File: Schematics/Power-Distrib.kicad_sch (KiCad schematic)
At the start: 43 parts, among them J10 Screw_Terminal_01x02, J11 Screw_Terminal_01x02, J12 Screw_Terminal_01x02, J13 Conn_01x03, J14 Conn_01x03, J15 Conn_01x03, J16 Conn_01x03, J17 Conn_01x02, J18 Conn_01x02, J19 Conn_01x02, J20 Conn_01x02, J21 Conn_01x02, J22 Conn_01x02, J23 Conn_01x02, J24 Conn_01x02, J25 Conn_01x03, J26 Conn_01x03, J27 Conn_01x03, J28 Conn_01x03, J29 Conn_01x03, U15 LM7805, U16 LM7812, U17 LM7912, U18 LM7805

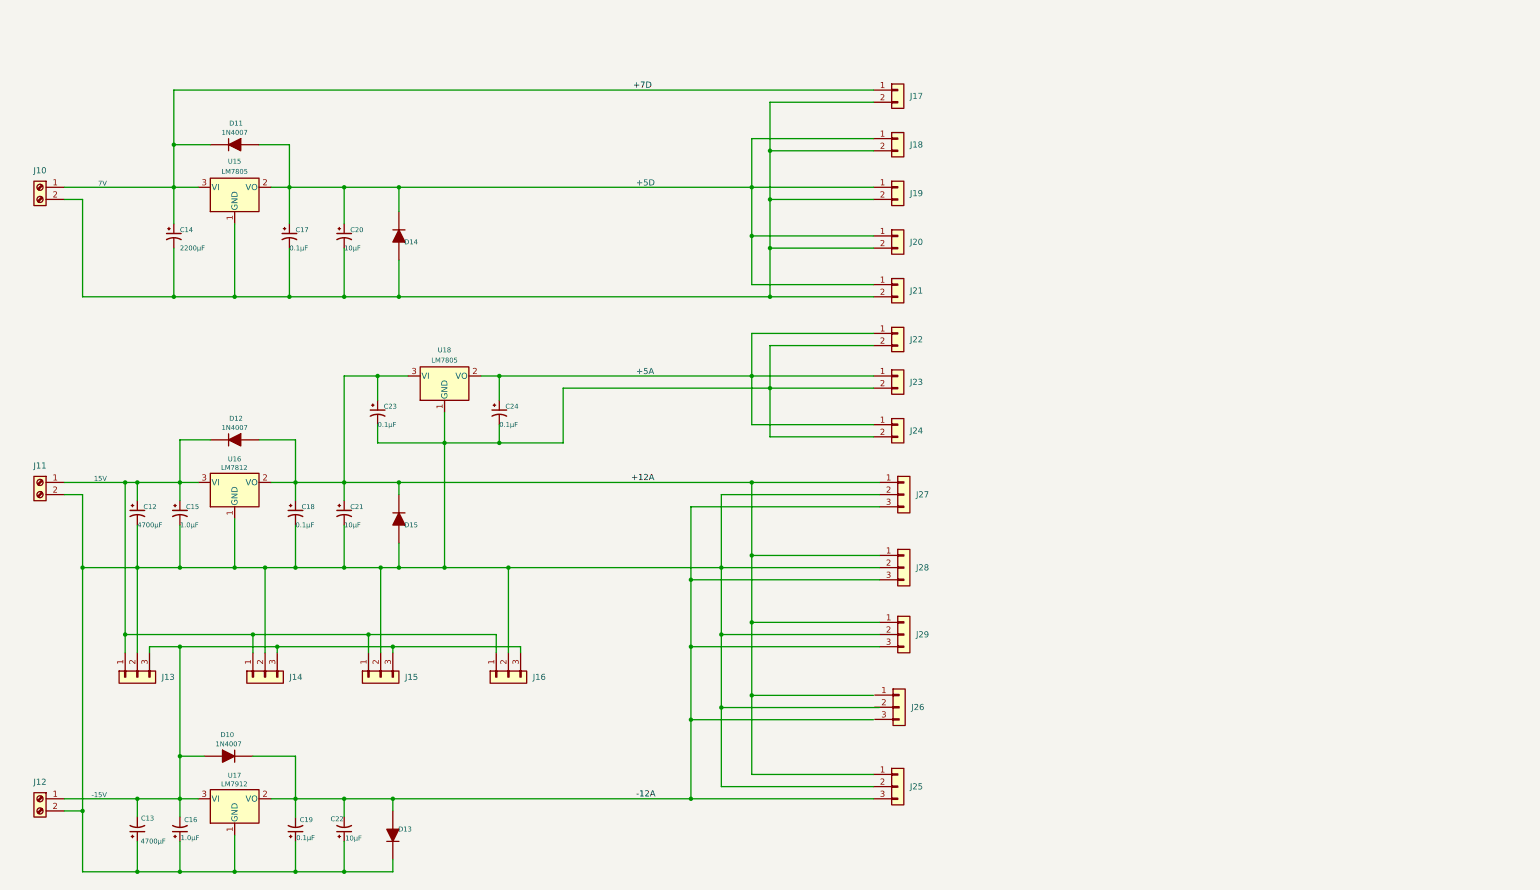
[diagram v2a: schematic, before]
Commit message: Partial software with complete hardware on best 3 state filter with 4 outputs.
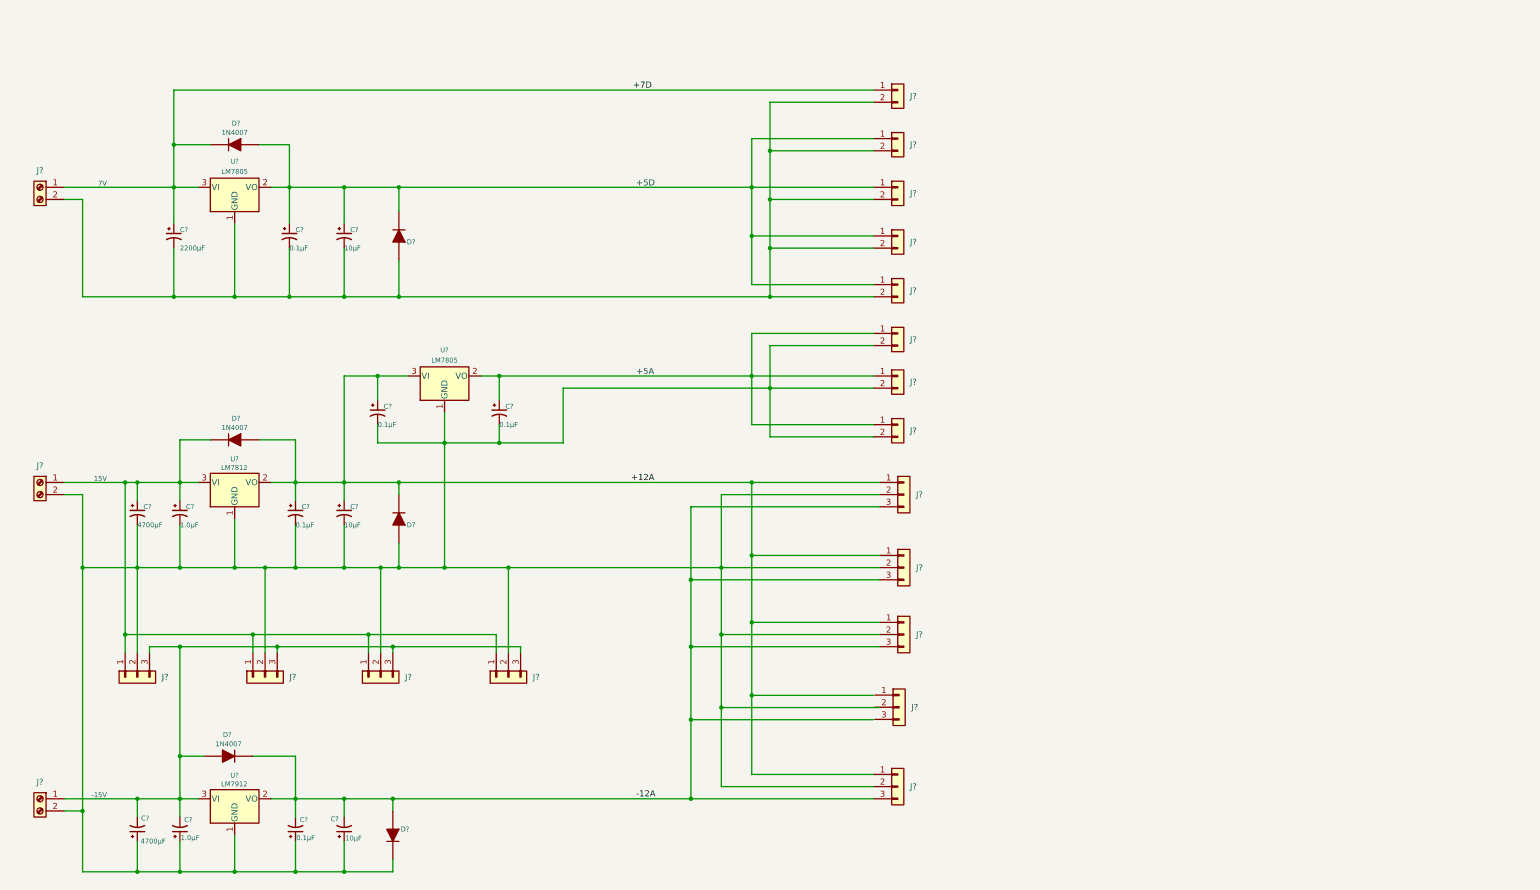
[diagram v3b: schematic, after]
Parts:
- renumbered C20 to C?, C12 to C?, C24 to C?, C13 to C?, C16 to C?, C23 to C?, C19 to C?, C18 to C?, C15 to C?, C22 to C?, C14 to C?, C17 to C?, C21 to C?, D11 to D?, D10 to D?, D13 to D?, D15 to D?, D14 to D?, D12 to D?, J28 to J?, J24 to J?, J27 to J?, J26 to J?, J20 to J?, J18 to J?, J13 to J?, J17 to J?, J22 to J?, J14 to J?, J25 to J?, J29 to J?, J11 to J?, J19 to J?, J21 to J?, J10 to J?, J23 to J?, J16 to J?, J15 to J?, J12 to J?, U15 to U?, U17 to U?, U18 to U?, U16 to U?

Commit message: - Updated current libraries - New 7 inc display with ESP32S3 and second USB upload port - Start of I2C feeder interface slave on display.
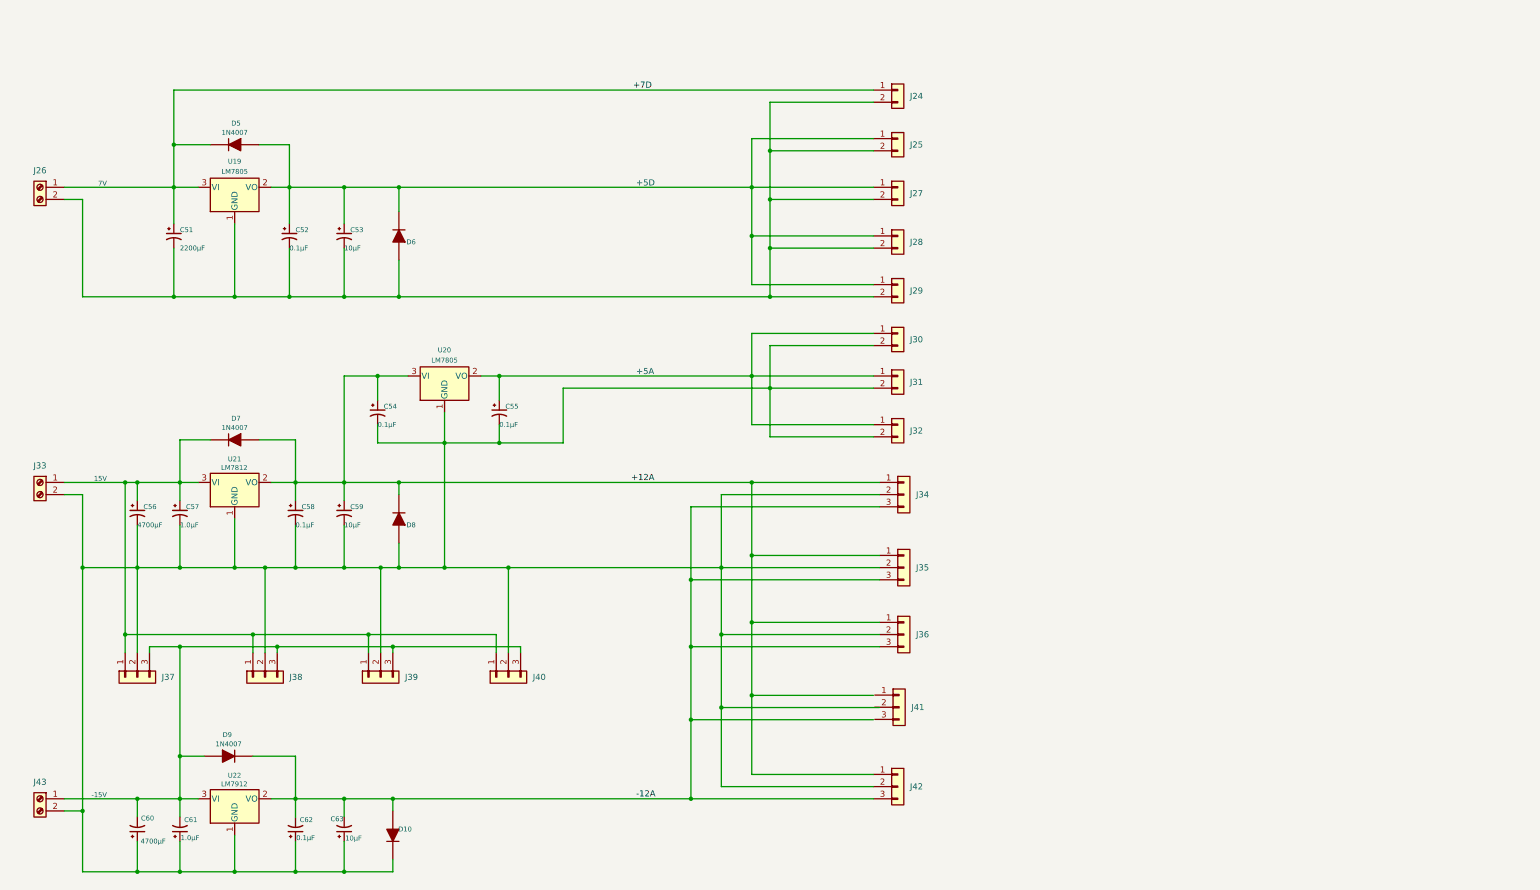
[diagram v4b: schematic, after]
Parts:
- gave numbers to parts that had none: 43

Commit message: Added LaunchControlXL
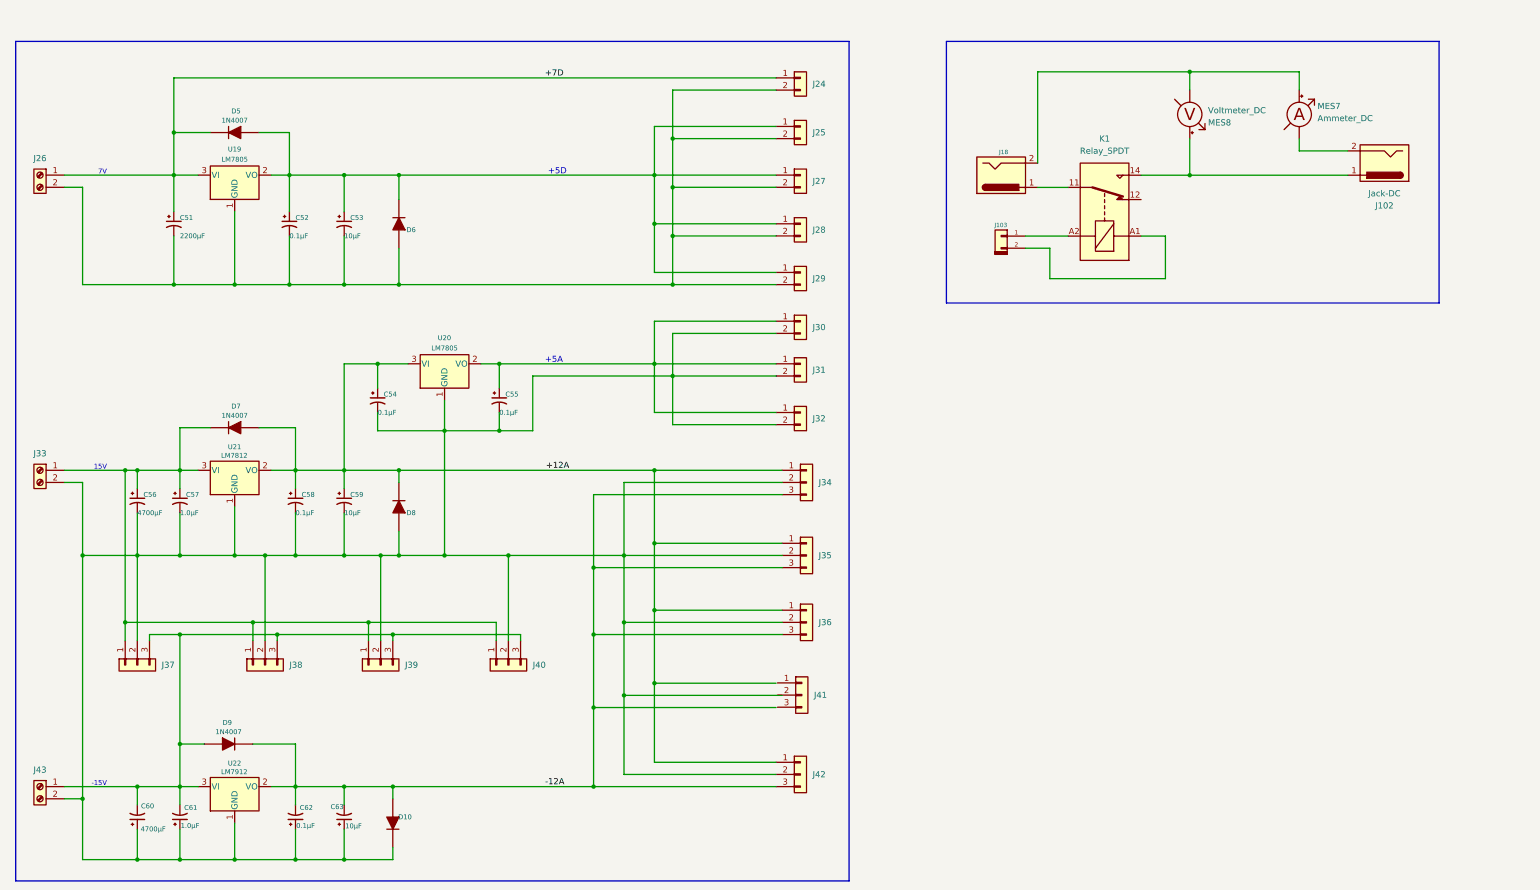
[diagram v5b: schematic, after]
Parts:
- added J102, J18: Jack-DC, symbol Connector:Jack-DC
- added J103: Conn_01x02, symbol My Connectors:Conn_01x02
- added K1: Relay_SPDT, symbol Relay:Relay_SPDT
- added MES7: Ammeter_DC, symbol Device:Ammeter_DC
- added MES8: Voltmeter_DC, symbol Device:Voltmeter_DC
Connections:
- new net: J18.1, K1.11
- new net: J18.2, MES7.2 (+), MES8.1 (-)
- new net: J102.1, K1.14, MES8.2 (+)
- new net: J103.1 (Pin_1), K1.A2
- new net: J103.2 (Pin_2), K1.A1
- new net: J102.2, MES7.1 (-)
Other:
- moved on the sheet: C51, C52, C53, C54, C55, C56, C57, C58, C59, C60, C61, C62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

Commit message: updated schematics.
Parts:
- removed J102, J18: Jack-DC, symbol Connector:Jack-DC
- removed J103: Conn_01x02, symbol My Connectors:Conn_01x02
- removed MES7: Ammeter_DC, symbol Device:Ammeter_DC
- removed MES8: Voltmeter_DC, symbol Device:Voltmeter_DC
- added C126, C128: 47µF, symbol Device:C_Polarized_Small_US
- added C127, C93: 0.1µF, symbol Device:C_Polarized_Small_US
- added C89, C92: 1000µF, symbol Device:C_Polarized_Small_US
- added C90, C91: 1.0µF, symbol Device:C_Polarized_Small_US
- added J10, J12: Jack-DC, symbol Connector:Jack-DC
- added J11: Conn_01x02, symbol My Connectors:Conn_01x02
- added J18, J52, J53: Conn_01x03, symbol Connector_Generic:Conn_01x03
- added MES7: Voltmeter_DC, symbol Device:Voltmeter_DC
- added MES8: Ammeter_DC, symbol Device:Ammeter_DC
- added U102: LM7812, symbol Regulator_Linear:LM1117-5.0
- added U104: LM7912, symbol Regulator_Linear:LM1117-5.0
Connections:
- net at K1.11: now also J10.1
- net at K1.14: now also J12.1, MES7.2 (+)
- net at K1.A2: now also J11.1 (Pin_1)
- net at K1.A1: now also J11.2 (Pin_2)
- new net: C126.2, C127.1, C128.1, C89.1, C90.1, C91.2, C92.2, C93.2, J18.3 (Pin_3), J52.3 (Pin_3), J53.1 (Pin_1), U102.1 (GND), U104.1 (GND)
- new net: C126.1, C93.1, J52.1 (Pin_1), J53.2 (Pin_2), U102.2 (VO)
- new net: C127.2, C128.2, J52.2 (Pin_2), J53.3 (Pin_3), U104.2 (VO)
- new net: C91.1, C92.1, J18.1 (Pin_1), U102.3 (VI)
- new net: C89.2, C90.2, J18.2 (Pin_2), U104.3 (VI)
- new net: J10.2, MES7.1 (-), MES8.2 (+)
- new net: J12.2, MES8.1 (-)
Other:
- note added: "12V 3A WallWart"
- note added: "12V to USB Hub"
- note added: "5V Control"
- moved on the sheet: C54, C56, C57, C58, C59, C60, C61, C62, C63, D10, D7, D9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

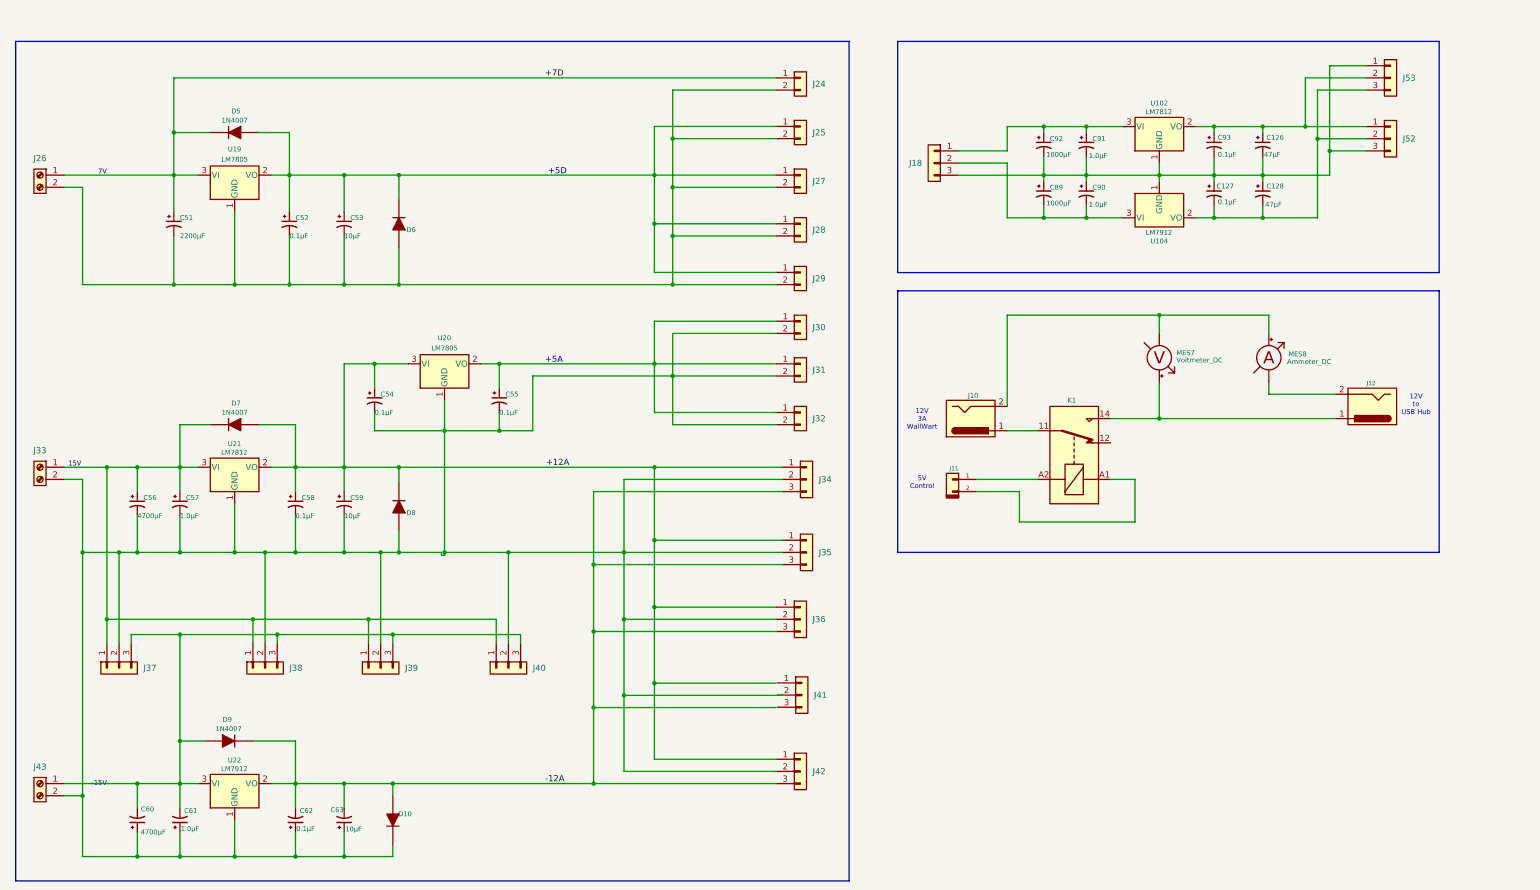
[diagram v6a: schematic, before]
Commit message: Upgreade byte value interface to short.  First stage of refactoring midi input for rotory encoders.  Still needs scaling.
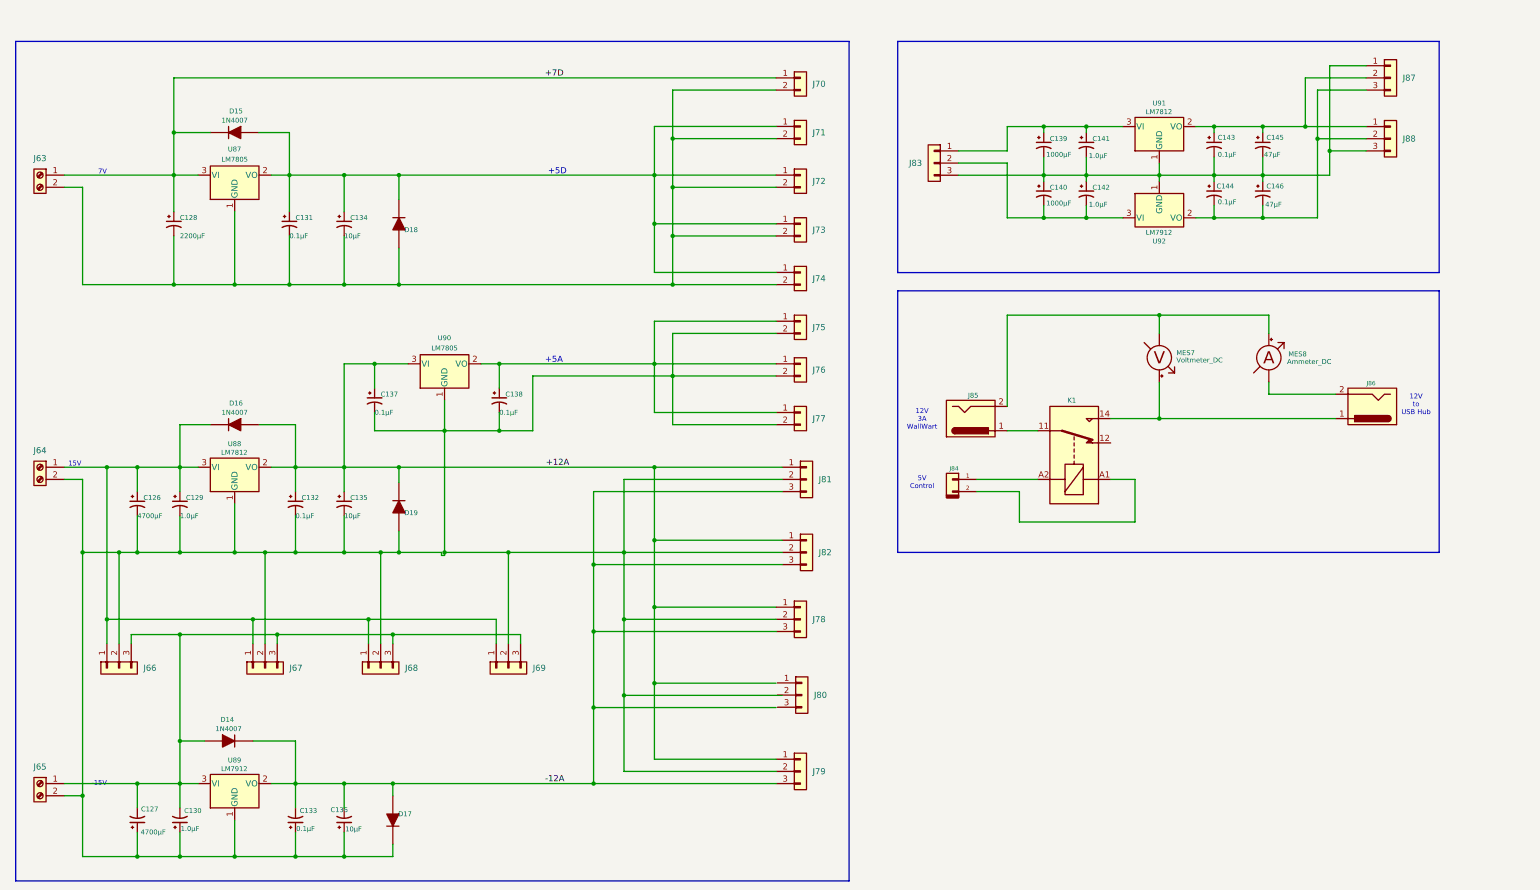
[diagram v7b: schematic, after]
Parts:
- renumbered C56 to C126, C60 to C127, C51 to C128, C57 to C129, C61 to C130, C52 to C131, C58 to C132, C62 to C133, C53 to C134, C59 to C135, C63 to C136, C54 to C137, C55 to C138, C92 to C139, C89 to C140, C91 to C141, C90 to C142, C93 to C143, C127 to C144, C126 to C145, C128 to C146, D9 to D14, D5 to D15, D7 to D16, D10 to D17, D6 to D18, D8 to D19, J26 to J63, J33 to J64, J43 to J65, J37 to J66, J38 to J67, J39 to J68, J40 to J69, J24 to J70, J25 to J71, J27 to J72, J28 to J73, J29 to J74, J30 to J75, J31 to J76, J32 to J77, J36 to J78, J42 to J79, J41 to J80, J34 to J81, J35 to J82, J18 to J83, J11 to J84, J10 to J85, J12 to J86, J53 to J87, J52 to J88, U19 to U87, U21 to U88, U22 to U89, U20 to U90, U102 to U91, U104 to U92
